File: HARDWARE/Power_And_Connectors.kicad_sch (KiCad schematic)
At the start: 26 parts, among them J1 USB_C_Receptacle_USB2.0_16P, U1 TCR2EF33_LMCT

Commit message: Update footprints and add all PNs
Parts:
- removed CH1, CH2, CH3, CH4, CH5, CH6: Conn_01x03, Connector_PinHeader_2.54mm:PinHeader_1x03_P2.54mm_Vertical, symbol Connector_Generic:Conn_01x03
- added J2: Conn_01x18, Connector_PinHeader_2.54mm_Custom:PinHeader_3x06_P2.54mm_Vertical, symbol Connector_Generic:Conn_01x18
- C1, C10, C3, C4, C5, C6, C7, C8, C9: Part Number (none) -> 1276-1102-2-ND
- C2: Part Number (none) -> 311-1341-2-ND
- CRSF1: footprint (none) -> Connector_PinHeader_2.54mm:PinHeader_1x04_P2.54mm_Vertical; Part Number (none) -> 732-5317-ND
- D1, D2: footprint (none) -> Diode_SMD:D_SOD-323_HandSoldering; Part Number (none) -> CUS520H3FTR-ND
- J1: Part Number (none) -> 2073-USB4105-GF-ATR-ND
- R1, R2: Part Number (none) -> 311-5.10KHRTR-ND
- R3: Part Number (none) -> 311-1.00KHRTR-ND
- SWD1: footprint Connector_PinSocket_1.27mm:PinSocket_2x05_P1.27mm_Vertical -> Connector_PinHeader_1.27mm:PinHeader_2x05_P1.27mm_Vertical; Part Number (none) -> S9015E-05-ND
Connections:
- net CH1_PWM: now also J2.1 (Pin_1)
- net CH2_PWM: now also J2.4 (Pin_4)
- net CH3_PWM: now also J2.7 (Pin_7)
- net CH4_PWM: now also J2.10 (Pin_10)
- net CH5_PWM: now also J2.13 (Pin_13)
- net CH6_PWM: now also J2.16 (Pin_16)
- net GND: now also C10.1, C6.1, C7.1, C8.1, C9.1, J2.12 (Pin_12), J2.15 (Pin_15), J2.18 (Pin_18), J2.3 (Pin_3), J2.6 (Pin_6), J2.9 (Pin_9); no longer C10.2, C6.2, C7.2, C8.2, C9.2
- net V_ESC: now also C10.2, C6.2, C7.2, C8.2, C9.2, J2.11 (Pin_11), J2.14 (Pin_14), J2.17 (Pin_17), J2.2 (Pin_2), J2.5 (Pin_5), J2.8 (Pin_8); no longer C10.1, C6.1, C7.1, C8.1, C9.1
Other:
- note added: "3x6 ESC/Servo PWM Header Row 1: PWM Row 2: +5V Row 3: GND This is one header so that KiCAD exports this as one item in the BOM instead of six separate headers because this is a single part"
- note added: "Amber LED Vf=1.8V If=2mA"
- note added: "Power ORing to prevent USB from powering ESC/servos and vice versa"
- moved on the sheet: C1, C2, C3, C4, CRSF1, D1, D2, J1, PWR1, R1, R2, R3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

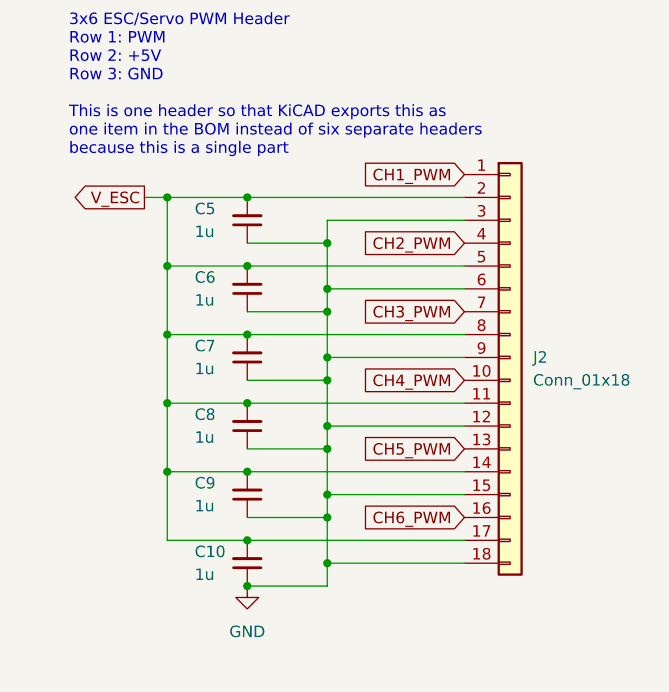
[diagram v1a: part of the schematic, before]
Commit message: Swap PWM channels and initial PCB layout
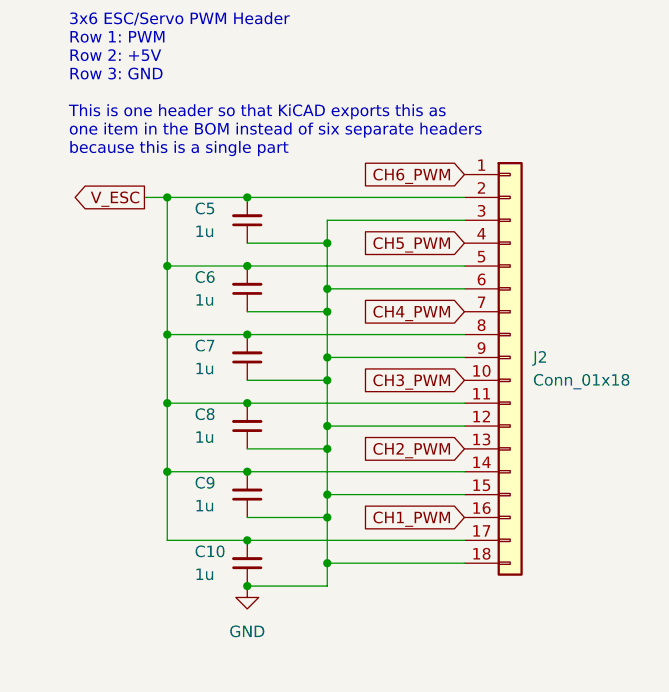
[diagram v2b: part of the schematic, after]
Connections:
- net CH1_PWM: now also J2.16 (Pin_16); no longer J2.1 (Pin_1)
- net CH2_PWM: now also J2.13 (Pin_13); no longer J2.4 (Pin_4)
- net CH3_PWM: now also J2.10 (Pin_10); no longer J2.7 (Pin_7)
- net CH4_PWM: now also J2.7 (Pin_7); no longer J2.10 (Pin_10)
- net CH5_PWM: now also J2.4 (Pin_4); no longer J2.13 (Pin_13)
- net CH6_PWM: now also J2.1 (Pin_1); no longer J2.16 (Pin_16)

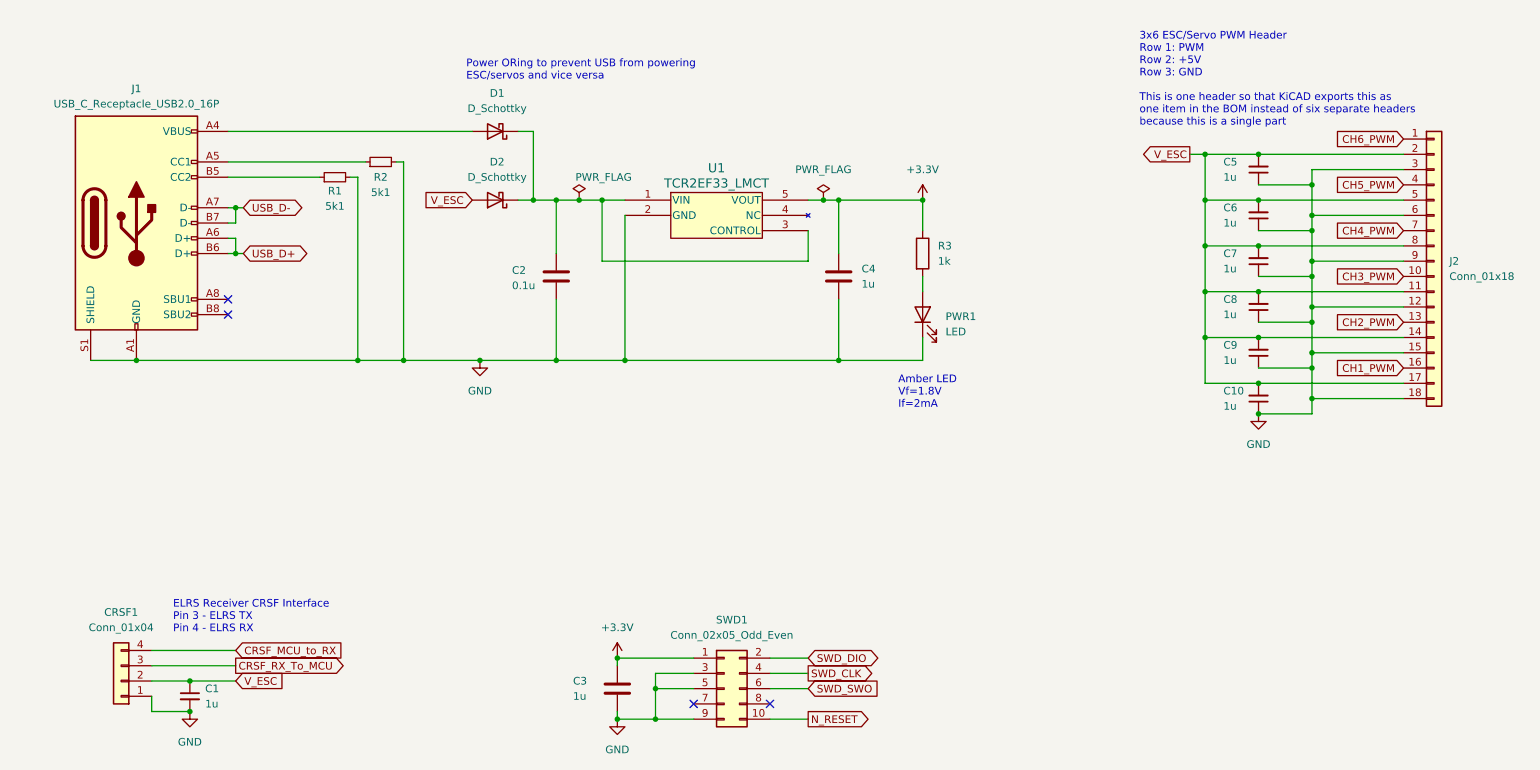
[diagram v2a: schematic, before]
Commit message: Update components and layout
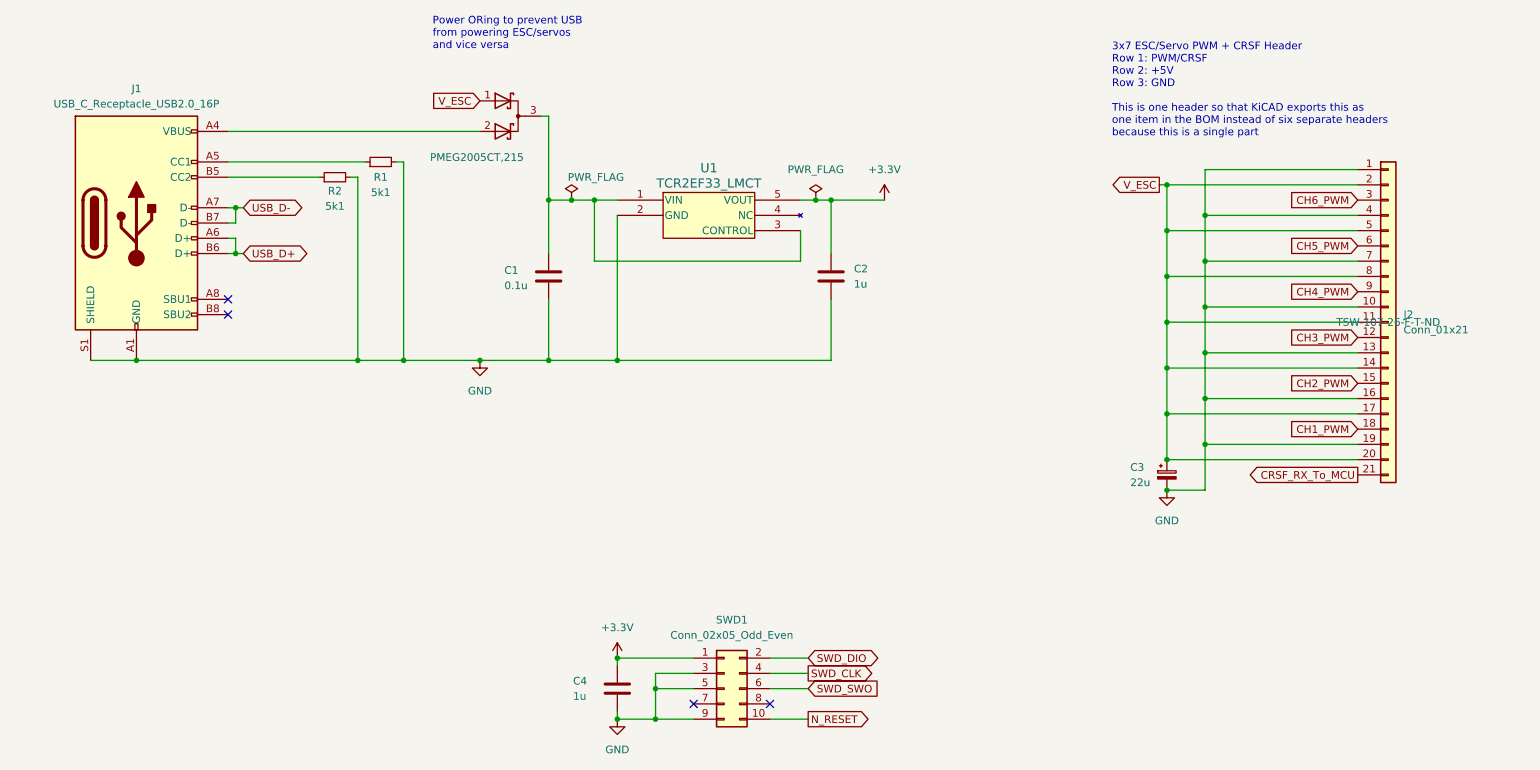
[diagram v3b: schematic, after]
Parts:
- removed C1, C10, C5, C6, C7, C8, C9: 1u, Capacitor_SMD:C_0603_1608Metric_Pad1.08x0.95mm_HandSolder, symbol Device:C_Small
- removed CRSF1: Conn_01x04, Connector_PinHeader_2.54mm:PinHeader_1x04_P2.54mm_Vertical, symbol Connector_Generic:Conn_01x04
- removed D1, D2: D_Schottky, Diode_SMD:D_SOD-323_HandSoldering, symbol Device:D_Schottky
- removed J2: Conn_01x18, Connector_PinHeader_2.54mm_Custom:PinHeader_3x06_P2.54mm_Vertical, symbol Connector_Generic:Conn_01x18
- removed PWR1: LED, LED_SMD:LED_1206_3216Metric_Pad1.42x1.75mm_HandSolder, symbol Device:LED
- removed R3: 1k, Resistor_SMD:R_0603_1608Metric_Pad0.98x0.95mm_HandSolder, symbol Device:R
- added C3: 22u, Capacitor_SMD:CP_Elec_4x5.4, symbol Device:C_Polarized_Small
- added D1: PMEG2005CT,215, Package_TO_SOT_SMD:SOT-23, symbol Device:D_Schottky_Dual_CommonCathode_AAK_Parallel
- added J2: Conn_01x21, Connector_PinHeader_2.54mm_Custom:PinHeader_3x07_P2.54mm_Vertical, symbol Connector_Generic:Conn_01x21
- C1: renamed from C2; footprint Capacitor_SMD:C_0603_1608Metric_Pad1.08x0.95mm_HandSolder -> Capacitor_SMD:C_0402_1005Metric_Pad0.74x0.62mm_HandSolder; MFN (none) -> CL05B104KA5NNNC; Part Number 311-1341-2-ND -> 1276-6720-1-ND
- C2: renamed from C4; footprint Capacitor_SMD:C_0603_1608Metric_Pad1.08x0.95mm_HandSolder -> Capacitor_SMD:C_0402_1005Metric_Pad0.74x0.62mm_HandSolder; MFN (none) -> CL05A105KA5NQNC; Part Number 1276-1102-2-ND -> 1276-1445-1-ND
- C4: renamed from C3; footprint Capacitor_SMD:C_0603_1608Metric_Pad1.08x0.95mm_HandSolder -> Capacitor_SMD:C_0402_1005Metric_Pad0.74x0.62mm_HandSolder; MFN (none) -> CL05A105KA5NQNC; Part Number 1276-1102-2-ND -> 1276-1445-1-ND
- J1: MFN (none) -> USB4105-GF-A
- R1: renamed from R2; footprint Resistor_SMD:R_0603_1608Metric_Pad0.98x0.95mm_HandSolder -> Resistor_SMD:R_0402_1005Metric_Pad0.72x0.64mm_HandSolder; MFN (none) -> RC0402FR-135K1L; Part Number 311-5.10KHRTR-ND -> 13-RC0402FR-135K1LCT-ND
- R2: renamed from R1; footprint Resistor_SMD:R_0603_1608Metric_Pad0.98x0.95mm_HandSolder -> Resistor_SMD:R_0402_1005Metric_Pad0.72x0.64mm_HandSolder; MFN (none) -> RC0402FR-135K1L; Part Number 311-5.10KHRTR-ND -> 13-RC0402FR-135K1LCT-ND
- SWD1: MFN (none) -> GRPB052VWVN-RC
- U1: MFN (none) -> TCR2EF33,LM(CT
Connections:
- net CH1_PWM: now also J2.18 (Pin_18)
- net CH2_PWM: now also J2.15 (Pin_15)
- net CH3_PWM: now also J2.12 (Pin_12)
- net CH4_PWM: now also J2.9 (Pin_9)
- net CH5_PWM: now also J2.6 (Pin_6)
- net CH6_PWM: now also J2.3 (Pin_3)
- net CRSF_RX_To_MCU: now also J2.21 (Pin_21)
- net GND: now also C3.2, J2.1 (Pin_1), J2.10 (Pin_10), J2.13 (Pin_13), J2.16 (Pin_16), J2.19 (Pin_19), J2.4 (Pin_4), J2.7 (Pin_7)
- net V_ESC: now also C3.1, D1.1 (A), J2.11 (Pin_11), J2.14 (Pin_14), J2.17 (Pin_17), J2.2 (Pin_2), J2.20 (Pin_20), J2.5 (Pin_5), J2.8 (Pin_8)
- net at C1.1, U1.1 (VIN), U1.3 (CONTROL): now also D1.3 (K)
- net at J1.A4 (VBUS), J1.A9 (VBUS), J1.B4 (VBUS)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: now also D1.2 (A)
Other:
- note added: "3x7 ESC/Servo PWM + CRSF Header Row 1: PWM/CRSF Row 2: +5V Row 3: GND This is one header so that KiCAD exports this as one item in the BOM instead of six separate headers because this is a single part"
- note removed: "3x6 ESC/Servo PWM Header Row 1: PWM Row 2: +5V Row 3: GND This is one header so that KiCAD exports this as one item in the BOM instead of six separate headers because this is a single part"
- note removed: "Amber LED Vf=1.8V If=2mA"
- note removed: "ELRS Receiver CRSF Interface Pin 3 - ELRS TX Pin 4 - ELRS RX"
- moved on the sheet: C1, C2, U1

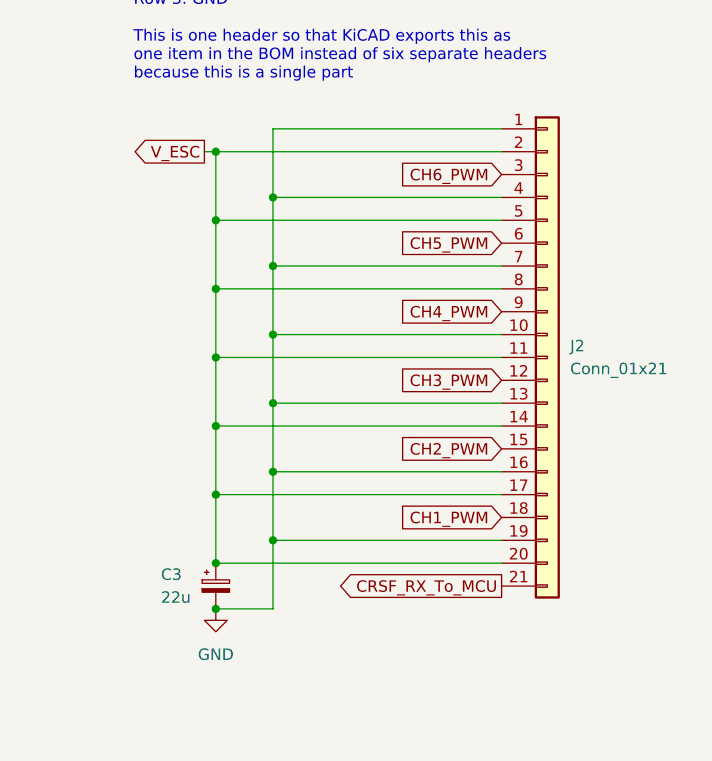
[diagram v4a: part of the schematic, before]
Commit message: Complete initial routing
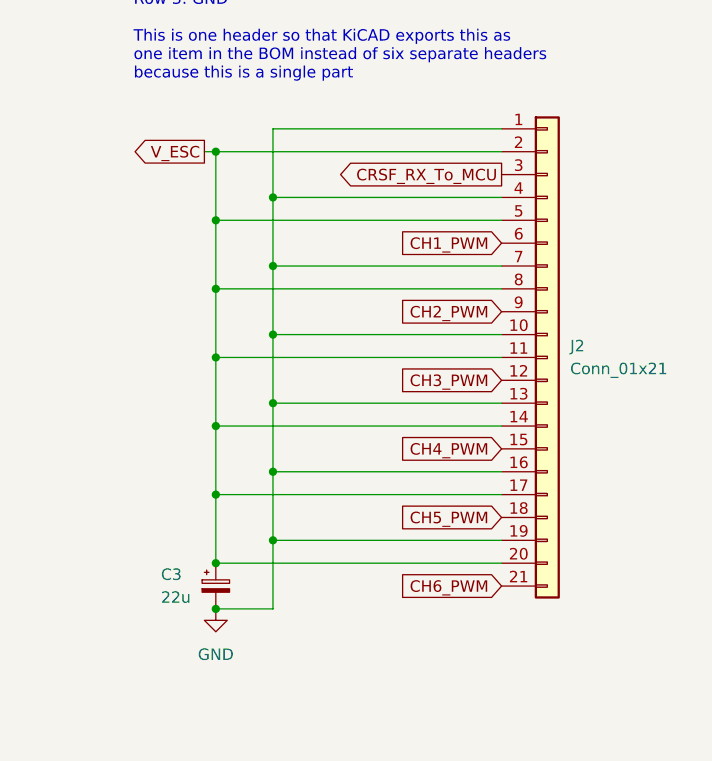
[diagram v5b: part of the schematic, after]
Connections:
- net CH1_PWM: now also J2.6 (Pin_6); no longer J2.18 (Pin_18)
- net CH2_PWM: now also J2.9 (Pin_9); no longer J2.15 (Pin_15)
- net CH4_PWM: now also J2.15 (Pin_15); no longer J2.9 (Pin_9)
- net CH5_PWM: now also J2.18 (Pin_18); no longer J2.6 (Pin_6)
- net CH6_PWM: now also J2.21 (Pin_21); no longer J2.3 (Pin_3)
- net CRSF_RX_To_MCU: now also J2.3 (Pin_3); no longer J2.21 (Pin_21)

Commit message: Add images and BOM CSV
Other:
- note added: "3x7 ESC/Servo PWM + CRSF Header Row 1: PWM/CRSF Row 2: +5V Row 3: GND This is one header so that KiCAD exports this as one item in the BOM instead of seven separate headers because this is a single part"
- note added: "Bulk capacitor for servos"
- note removed: "3x7 ESC/Servo PWM + CRSF Header Row 1: PWM/CRSF Row 2: +5V Row 3: GND This is one header so that KiCAD exports this as one item in the BOM instead of six separate headers because this is a single part"

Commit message: Add other fields to BOM
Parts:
- C1: DigiKey Part # (none) -> 1276-6720-1-ND; MANUFACTURER (none) -> Samsung Electro-Mechanics; MFN CL05B104KA5NNNC -> (none); Mfg Part # (none) -> CL05B104KA5NNNC; Package (none) -> 0402; Part Number 1276-6720-1-ND -> (none)
- C2, C4: DigiKey Part # (none) -> 1276-1445-1-ND; MANUFACTURER (none) -> Samsung Electro-Mechanics; MFN CL05A105KA5NQNC -> (none); Mfg Part # (none) -> CL05A105KA5NQNC; Package (none) -> 0402; Part Number 1276-1445-1-ND -> (none)
- C3: DigiKey Part # (none) -> 732-8413-1-ND; MANUFACTURER (none) -> Würth Elektronik; MFN 865080340003 -> (none); Mfg Part # (none) -> 865080340003; Package (none) -> Radial, Can - SMD; Part Number 732-8413-1-ND -> (none)
- D1: DigiKey Part # (none) -> 1727-5188-2-ND; MANUFACTURER (none) -> Nexperia USA Inc.; MFN PMEG2005CT,215 -> (none); Mfg Part # (none) -> PMEG2005CT,215; Package (none) -> 3-SOT; Part Number 1727-5188-2-ND -> (none)
- J1: DigiKey Part # (none) -> 2073-USB4105-GF-ATR-ND; MANUFACTURER (none) -> GCT; MFN USB4105-GF-A -> (none); Mfg Part # (none) -> USB4105-GF-A; Package (none) -> USB-C; Part Number 2073-USB4105-GF-ATR-ND -> (none)
- J2: DigiKey Part # (none) -> TSW-107-26-F-T-ND; MANUFACTURER (none) -> Samtec Inc.; MFN TSW-107-26-F-T -> (none); Mfg Part # (none) -> TSW-107-26-F-T; Package (none) -> 21POS; Part Number TSW-107-26-F-T-ND -> (none)
- R1, R2: DigiKey Part # (none) -> 13-RC0402FR-135K1LCT-ND; MANUFACTURER (none) -> YAGEO; MFN RC0402FR-135K1L -> (none); Mfg Part # (none) -> RC0402FR-135K1L; Package (none) -> 0402; Part Number 13-RC0402FR-135K1LCT-ND -> (none)
- SWD1: DigiKey Part # (none) -> S9015E-05-ND; MANUFACTURER (none) -> Sullins Connector Solutions; MFN GRPB052VWVN-RC -> (none); Mfg Part # (none) -> GRPB052VWVN-RC; Package (none) -> 10POS; Part Number S9015E-05-ND -> (none)
- U1: DigiKey Part # (none) -> TCR2EF33LM(CTTR-ND; MANUFACTURER (none) -> Toshiba Semiconductor and Storage; MFN TCR2EF33,LM(CT -> (none); Mfg Part # (none) -> TCR2EF33,LM(CT; Package (none) -> 5-SOT; Part Number TCR2EF33LM(CTTR-ND -> (none)
